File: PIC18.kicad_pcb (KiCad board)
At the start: 4 copper layers, 76.6 x 75.6 mm, 75 parts, among them J1 Conn_02x20_Odd_Even, J10 Port B, J11 Port C, J12 Port D, J13 Conn_01x03, J14 Conn_01x03, J15 Conn_01x03, J16 Conn_01x03, J2 Conn_01x06, J3 USB_A, J4 Conn_01x03, J5 Conn_01x02, J6 Conn_01x02, J7 USB_OTG, J8 Port A, J9 Port E, U1 PIC18F4620, U2 LM4040DBZ-4.1, U3 FT230XS, Y1 8 MHz

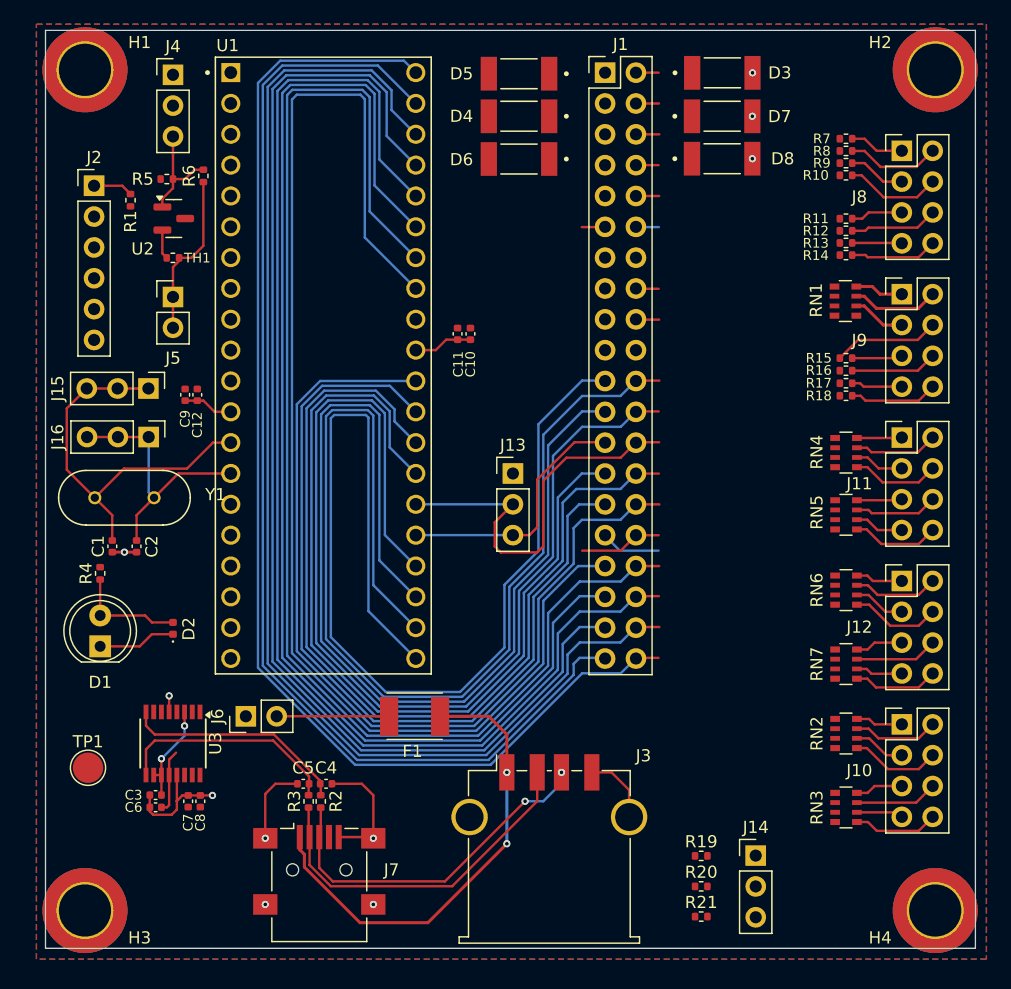
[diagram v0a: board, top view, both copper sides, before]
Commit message: Header Wiring
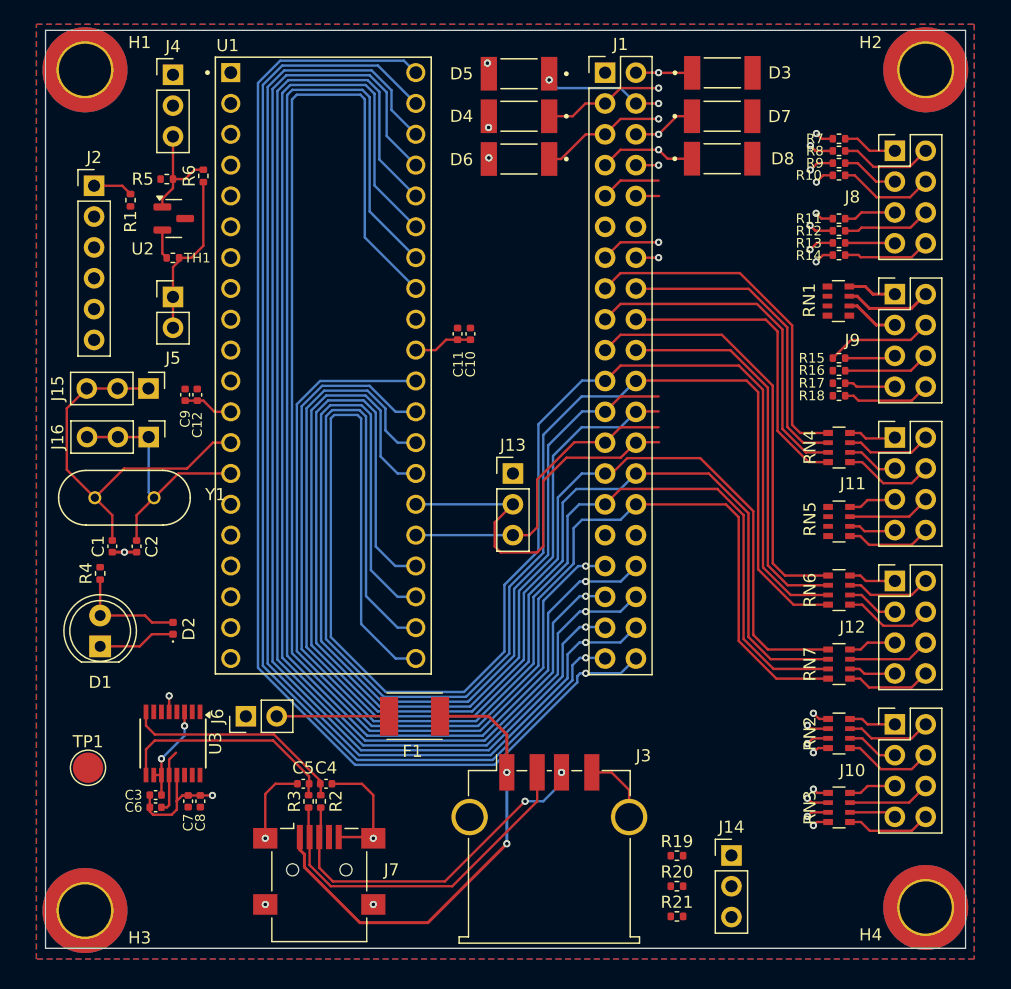
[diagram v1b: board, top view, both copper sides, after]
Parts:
- moved J14 2.00 mm to (156.0, 133.5)
- moved R19 2.00 mm to (151.5, 133.5)
- moved R20 2.00 mm to (151.5, 136.0)
- moved R21 2.00 mm to (151.5, 138.5)
- moved H4 0.82 mm to (172.0, 137.8)
- moved RN5 0.80 mm to (164.9, 106.0)
- moved H2 0.78 mm to (172.0, 68.8)
- moved RN4 0.71 mm to (164.9, 99.9)
- moved J10 0.57 mm to (169.5, 122.7)
- moved J11 0.57 mm to (169.5, 99.0)
- moved J12 0.57 mm to (169.5, 110.9)
- moved J8 0.57 mm to (169.5, 75.4)
- moved J9 0.57 mm to (169.5, 87.2)
- moved R10 0.57 mm to (164.9, 77.4)
- moved R11 0.57 mm to (164.9, 81.0)
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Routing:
- net /RB1/INT1/AN10: track 109.9 -> 149.0 mm, vias 0 -> 2
- net /RB0/INT0/FLT0/AN12: track 111.3 -> 149.9 mm, vias 0 -> 2
- net /RB3/AN9/CCP2(1): track 107.0 -> 140.8 mm, vias 0 -> 2
- net /RB2/INT2/AN8: track 108.5 -> 141.6 mm, vias 0 -> 2
- net /RD1/PSP1: track 56.3 -> 88.1 mm
- net /RD0/PSP0: track 55.6 -> 86.9 mm
- net /RD2/PSP2: track 91.9 -> 123.1 mm
- net /RD3/PSP3: track 90.5 -> 121.3 mm
- net /RB5/KBI1/PGM: track 104.1 -> 131.4 mm, vias 0 -> 2
- net /RD4/PSP4: track 78.3 -> 105.5 mm
- net /RC0/T1OSO/T13CKI: track 48.2 -> 75.3 mm
- net /RD5/PSP5/P1B: track 77.1 -> 104.0 mm
- net /RB4/KBI0/AN11: track 105.5 -> 132.0 mm, vias 0 -> 2
- net /RD6/PSP6/P1C: track 76.1 -> 102.3 mm
- net /RD7/PSP7/P1D: track 75.7 -> 101.7 mm
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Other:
- board size 76.6 x 75.6 mm -> 75.8 x 75.6 mm

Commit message: All main wiring done
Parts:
- moved R21 1.23 mm to (152.7, 138.5)
- moved R19 1.23 mm to (152.7, 133.5)
- moved R20 1.23 mm to (152.7, 136.0)
- moved J13 0.34 mm to (137.7, 102.0)
- moved J4 0.10 mm to (110.0, 69.3)
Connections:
- J13 pad 1: GND -> unconnected-(J13-Pin_1-Pad1)
- J13 pad 2: /RC7/RX/DT -> /ICTX
- J4 pad 2: /VREF+ -> /RA3/AN3/VREF+
- J4 pad 3: Net-(J4-Pin_3) -> /VREF+
- R5 pad 2: Net-(J4-Pin_3) -> /VREF+
- R6 pad 2: Net-(J4-Pin_3) -> /VREF+
- U2 pad 1: Net-(J4-Pin_3) -> /VREF+
- U3 pad 1: /RC7/RX/DT -> /ICTX
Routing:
- net /RC6/TX/CK: track 26.0 -> 155.3 mm, vias 0 -> 2
- net /VREF+: track 8.78 -> 106.8 mm, vias 0 -> 4
- net /RC7/RX/DT: track 32.7 -> 114.1 mm, vias 0 -> 2
- net /RC4/SDI/SDA: track 89.6 -> 149.7 mm, vias 0 -> 2
- net /RC5/SDO: track 88.2 -> 143.9 mm, vias 0 -> 2
- net /RC3/SCK/SCL: track 78.0 -> 130.1 mm
- net /ICTX: track 0.00 -> 39.8 mm, vias 0 -> 1
- net /RB6/KBI2/PGC: track 124.4 -> 158.1 mm, vias 2 -> 3
- net /RB7/KBI3/PGD: track 124.8 -> 158.4 mm, vias 2 -> 3
- net GND: track 53.8 -> 76.9 mm, vias 10 -> 11
- net /RE0/RD*/AN5: track 39.4 -> 57.5 mm, vias 1 -> 2
- net /RE1/WR*/AN6: track 40.0 -> 57.7 mm, vias 0 -> 2
- net /RE2/CS*/AN7: track 40.5 -> 58.1 mm, vias 0 -> 2
- net /*MCLR/VPP/RE3: track 35.2 -> 52.5 mm
- net Net-(J4-Pin_3): track 8.99 -> 0.00 mm
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
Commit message: Edited PCB
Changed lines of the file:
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@@
 	)
 	(segment
+		(start 137.65625 107.08)
+		(end 130 107.08)
+		(width 0.2)
+		(layer "In2.Cu")
+		(net 24)
+	)
+	(segment
 		(start 138.025 111.47482)
 		(end 140.825 108.67482)
@@
 	)
 	(segment
-		(start 137.65625 107.08)
-		(end 130 107.08)
-		(width 0.2)
-		(layer "B.Cu")
-		(net 24)
-	)
-	(segment
 		(start 122.968628 96.4)
 		(end 121.45 97.918628)
@@
 	)
 	(zone
-		(net 24)
-		(net_name "/RC6{slash}TX{slash}CK")
-		(layer "F.Cu")
-		(name "$teardrop_padvia$")
-		(hatch full 0.1)
-		(priority 30104)
-		(attr
-			(teardrop
-				(type padvia)
-			)
-		)
-		(connect_pads yes
-			(clearance 0)
-		)
-		(min_thickness 0.0254)
-		(filled_areas_thickness no)
-		(fill yes
-			(thermal_gap 0.5)
-			(thermal_bridge_width 0.5)
-			(island_removal_mode 1)
-			(island_area_min 10)
-		)
-		(polygon
-			(pts
-				(xy 128.815596 108.122982) (xy 128.957018 108.264404) (xy 130.301363 107.807555) (xy 130.000707 107.079293)
-				(xy 129.272445 106.778637)
-			)
-		)
-	)
-	(zone
 		(net 1)
 		(net_name "GND")
@@
 	)
 	(zone
+		(net 24)
+		(net_name "/RC6{slash}TX{slash}CK")
+		(layer "F.Cu")
+		(name "$teardrop_padvia$")
+		(hatch full 0.1)
+		(priority 30000)
+		(attr
+			(teardrop
+				(type padvia)
+			)
+		)
+		(connect_pads yes
+			(clearance 0)
+		)
+		(min_thickness 0.0254)
+		(filled_areas_thickness no)
+		(fill yes
+			(thermal_gap 0.5)
+			(thermal_bridge_width 0.5)
+			(island_removal_mode 1)
+			(island_area_min 10)
+		)
+		(polygon
+			(pts
+				(xy 128.815596 108.122982) (xy 128.957018 108.264404) (xy 130.301363 107.807555) (xy 130.000707 107.079293)
+				(xy 129.272445 106.778637)
+			)
+		)
+	)
+	(zone
 		(net 17)
 		(net_name "/RB7{slash}KBI3{slash}PGD")
@@
 	)
 	(zone
+		(net 24)
+		(net_name "/RC6{slash}TX{slash}CK")
+		(layer "In2.Cu")
+		(name "$teardrop_padvia$")
+		(hatch full 0.1)
+		(priority 30001)
+		(attr
+			(teardrop
+				(type padvia)
+			)
+		)
+		(connect_pads yes
+			(clearance 0)
+		)
+		(min_thickness 0.0254)
+		(filled_areas_thickness no)
+		(fill yes
+			(thermal_gap 0.5)
+			(thermal_bridge_width 0.5)
+			(island_removal_mode 1)
+			(island_area_min 10)
+		)
+		(polygon
+			(pts
+				(xy 131.575 107.18) (xy 131.575 106.98) (xy 130.301363 106.352445) (xy 129.999 107.08) (xy 130.301363 107.807555)
+			)
+		)
+	)
+	(zone
 		(net 38)
 		(net_name "/RA0{slash}AN0")
@@
 	)
 	(zone
+		(net 24)
+		(net_name "/RC6{slash}TX{slash}CK")
+		(layer "In2.Cu")
+		(name "$teardrop_padvia$")
+		(hatch full 0.1)
+		(priority 30000)
+		(attr
+			(teardrop
+				(type padvia)
+			)
+		)
+		(connect_pads yes
+			(clearance 0)
+		)
+		(min_thickness 0.0254)
+		(filled_areas_thickness no)
+		(fill yes
+			(thermal_gap 0.5)
+			(thermal_bridge_width 0.5)
+			(island_removal_mode 1)
+			(island_area_min 10)
+		)
+		(polygon
+			(pts
+				(xy 135.95625 106.98) (xy 135.95625 107.18) (xy 137.330969 107.865298) (xy 137.65725 107.08) (xy 137.330969 106.294702)
+			)
+		)
+	)
+	(zone
 		(net 20)
 		(net_name "/RA2{slash}AN2{slash}VREF-{slash}CVREF")
@@
 	)
 	(zone
-		(net 31)
-		(net_name "/RD6{slash}PSP6{slash}P1C")
+		(net 24)
+		(net_name "/RC6{slash}TX{slash}CK")
 		(layer "B.Cu")
 		(name "$teardrop_padvia$")
 		(hatch full 0.1)
-		(priority 30011)
+		(priority 30000)
 		(attr
 			(teardrop
@@
 		(polygon
 			(pts
-				(xy 143.892997 104.4475) (xy 143.892997 104.6475) (xy 145.267219 105.330298) (xy 145.5935 104.545)
-				(xy 145.267219 103.759702)
+				(xy 128.957018 105.895596) (xy 128.815596 106.037018) (xy 129.272445 107.381363) (xy 130.000707 107.080707)
+				(xy 130.301363 106.352445)
 			)
 		)
 	)
 	(zone
-		(net 17)
-		(net_name "/RB7{slash}KBI3{slash}PGD")
+		(net 31)
+		(net_name "/RD6{slash}PSP6{slash}P1C")
 		(layer "B.Cu")
 		(name "$teardrop_padvia$")
 		(hatch full 0.1)
-		(priority 30037)
+		(priority 30011)
 		(attr
 			(teardrop
@@
 		(polygon
 			(pts
-				(xy 128.830928 67.9) (xy 128.830928 68.1) (xy 129.272445 69.281363) (xy 130.001 68.98) (xy 130.301363 68.252445)
+				(xy 143.892997 104.4475) (xy 143.892997 104.6475) (xy 145.267219 105.330298) (xy 145.5935 104.545)
+				(xy 145.267219 103.759702)
 			)
 		)
 	)
 	(zone
-		(net 24)
-		(net_name "/RC6{slash}TX{slash}CK")
+		(net 17)
+		(net_name "/RB7{slash}KBI3{slash}PGD")
 		(layer "B.Cu")
 		(name "$teardrop_padvia$")
 		(hatch full 0.1)
-		(priority 30001)
+		(priority 30037)
 		(attr
 			(teardrop
@@
 		(polygon
 			(pts
-				(xy 143.8925 99.365) (xy 143.8925 99.565) (xy 145.267219 100.250298) (xy 145.5935 99.465) (xy 145.267219 98.679702)
+				(xy 128.830928 67.9) (xy 128.830928 68.1) (xy 129.272445 69.281363) (xy 130.001 68.98) (xy 130.301363 68.252445)
 			)
 		)
 	)
 	(zone
-		(net 9)
-		(net_name "/RD7{slash}PSP7{slash}P1D")
+		(net 24)
+		(net_name "/RC6{slash}TX{slash}CK")
 		(layer "B.Cu")
 		(name "$teardrop_padvia$")
 		(hatch full 0.1)
-		(priority 30008)
+		(priority 30001)
 		(attr
 			(teardrop
@@
 		(polygon
 			(pts
-				(xy 146.861207 105.677372) (xy 147.002628 105.818793) (xy 148.457781 105.330298) (xy 148.133207 104.544293)
-				(xy 147.347202 104.219719)
+				(xy 143.8925 99.365) (xy 143.8925 99.565) (xy 145.267219 100.250298) (xy 145.5935 99.465) (xy 145.267219 98.679702)
 			)
 		)
 	)
 	(zone
-		(net 23)
-		(net_name "/RD5{slash}PSP5{slash}P1B")
+		(net 9)
+		(net_name "/RD7{slash}PSP7{slash}P1D")
 		(layer "B.Cu")
 		(name "$teardrop_padvia$")
 		(hatch full 0.1)
-		(priority 30035)
+		(priority 30008)
 		(attr
 			(teardrop
@@
 		(polygon
 			(pts
-				(xy 128.517677 99.336257) (xy 128.376257 99.477677) (xy 129.698637 100.187555) (xy 130.000707 99.460707)
-				(xy 129.698637 98.732445)
+				(xy 146.861207 105.677372) (xy 147.002628 105.818793) (xy 148.457781 105.330298) (xy 148.133207 104.544293)
+				(xy 147.347202 104.219719)
 			)
 		)
 	)
 	(zone
-		(net 24)
-		(net_name "/RC6{slash}TX{slash}CK")
+		(net 23)
+		(net_name "/RD5{slash}PSP5{slash}P1B")
 		(layer "B.Cu")
 		(name "$teardrop_padvia$")
 		(hatch full 0.1)
-		(priority 30003)
+		(priority 30035)
 		(attr
 			(teardrop
@@
 		(polygon
 			(pts
-				(xy 135.95625 106.98) (xy 135.95625 107.18) (xy 137.330969 107.865298) (xy 137.65725 107.08) (xy 137.330969 106.294702)
+				(xy 128.517677 99.336257) (xy 128.376257 99.477677) (xy 129.698637 100.187555) (xy 130.000707 99.460707)
+				(xy 129.698637 98.732445)
 			)
 		)
@@
 	)
 	(zone
-		(net 24)
-		(net_name "/RC6{slash}TX{slash}CK")
-		(layer "B.Cu")
-		(name "$teardrop_padvia$")
-		(hatch full 0.1)
-		(priority 30032)
-		(attr
-			(teardrop
-				(type padvia)
-			)
-		)
-		(connect_pads yes
-			(clearance 0)
-		)
-		(min_thickness 0.0254)
-		(filled_areas_thickness no)
-		(fill yes
-			(thermal_gap 0.5)
-			(thermal_bridge_width 0.5)
-			(island_removal_mode 1)
-			(island_area_min 10)
-		)
-		(polygon
-			(pts
-				(xy 131.575 107.18) (xy 131.575 106.98) (xy 130.301363 106.352445) (xy 129.999 107.08) (xy 130.301363 107.807555)
-			)
-		)
-	)
-	(zone
 		(net 6)
 		(net_name "/RB5{slash}KBI1{slash}PGM")
@@
 			)
 		)
-	)
-	(zone
-		(net 24)
-		(net_name "/RC6{slash}TX{slash}CK")
-		(layer "B.Cu")
-		(name "$teardrop_padvia$")
-		(hatch full 0.1)
-		(priority 30025)
-		(attr
-			(teardrop
-				(type padvia)
-			)
-		)
-		(connect_pads yes
-			(clearance 0)
-		)
-		(min_thickness 0.0254)
-		(filled_areas_thickness no)
-		(fill yes
-			(thermal_gap 0.5)
-			(thermal_bridge_width 0.5)
-			(island_removal_mode 1)
-			(island_area_min 10)
-		)
-		(polygon
-			(pts
-				(xy 128.957018 105.895596) (xy 128.815596 106.037018) (xy 129.272445 107.381363) (xy 130.000707 107.080707)
-				(xy 130.301363 106.352445)
-			)
-		)

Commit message: Silkscreen edits
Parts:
- moved J6 1.77 mm to (117.5, 123.0)
- moved F1 1.00 mm to (129.9, 123.0)
- moved J2 0.98 mm to (103.0, 77.5)
- moved H3 0.90 mm to (102.0, 138.5)
- moved H4 0.90 mm to (172.5, 138.5)
- moved H1 0.79 mm to (102.0, 69.0)
- moved H2 0.56 mm to (172.5, 69.0)
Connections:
- net /ICTX renamed /TXD
- J13 pad 3: /RC6/TX/CK -> /RC7/RX/DT
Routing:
- net /RC7/RX/DT: track 114.1 -> 124.0 mm
- net /RC6/TX/CK: track 155.3 -> 148.7 mm
- net /RB3/AN9/CCP2(1): track 140.7 -> 146.2 mm, vias 2 -> 0
- net /RB1/INT1/AN10: track 148.0 -> 153.5 mm, vias 2 -> 0
- net /RB7/KBI3/PGD: track 158.4 -> 163.2 mm, vias 3 -> 1
- net /RB5/KBI1/PGM: track 130.5 -> 135.1 mm, vias 2 -> 0
- net /RB0/INT0/FLT0/AN12: track 148.9 -> 151.2 mm, vias 2 -> 0
- net /RB2/INT2/AN8: track 141.4 -> 143.7 mm, vias 2 -> 0
- net /RB6/KBI2/PGC: track 158.1 -> 159.8 mm, vias 3 -> 1
- net /RB4/KBI0/AN11: track 131.2 -> 132.7 mm, vias 2 -> 0
- net VCC: track 18.6 -> 17.1 mm
- net GND: track 76.9 -> 75.5 mm, vias 11 -> 13
- net Net-(J3-VBUS): track 32.7 -> 31.7 mm
- net /RD2/PSP2: track 117.2 -> 118.0 mm
- net /RD3/PSP3: track 115.4 -> 116.2 mm
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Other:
- board size 75.8 x 75.6 mm -> 76.5 x 75.5 mm
- board text added: "+5V"
- board text added: "Designed by pixelated_knight"
- board text added: "ICTX"
- board text added: "MC VREF+"
- board text added: "MCRX"
- board text added: "PICKIT4"
- board text added: "PORT A"
- board text added: "PORT B"
- board text added: "PORT C"
- board text added: "PORT D"
- board text added: "PORT E"
- board text added: "SCL"
- board text added: "SDI"
- board text added: "SDO"
- board text added: "VREF+"
- board text added: "VTH"

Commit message: JLCPCB parody edits
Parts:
- C10, C12: value .1uf -> 100nf

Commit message: more jlcpcb parody
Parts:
- D2: footprint LED_SMD:LED_0402_1005Metric -> LED_SMD:LED_0805_2012Metric
- R2, R3: value 27 -> 33
- moved D2 0.19 mm to (110.0, 114.9)

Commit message: prod
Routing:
- net /RD7/PSP7/P1D: track 102.2 -> 101.6 mm

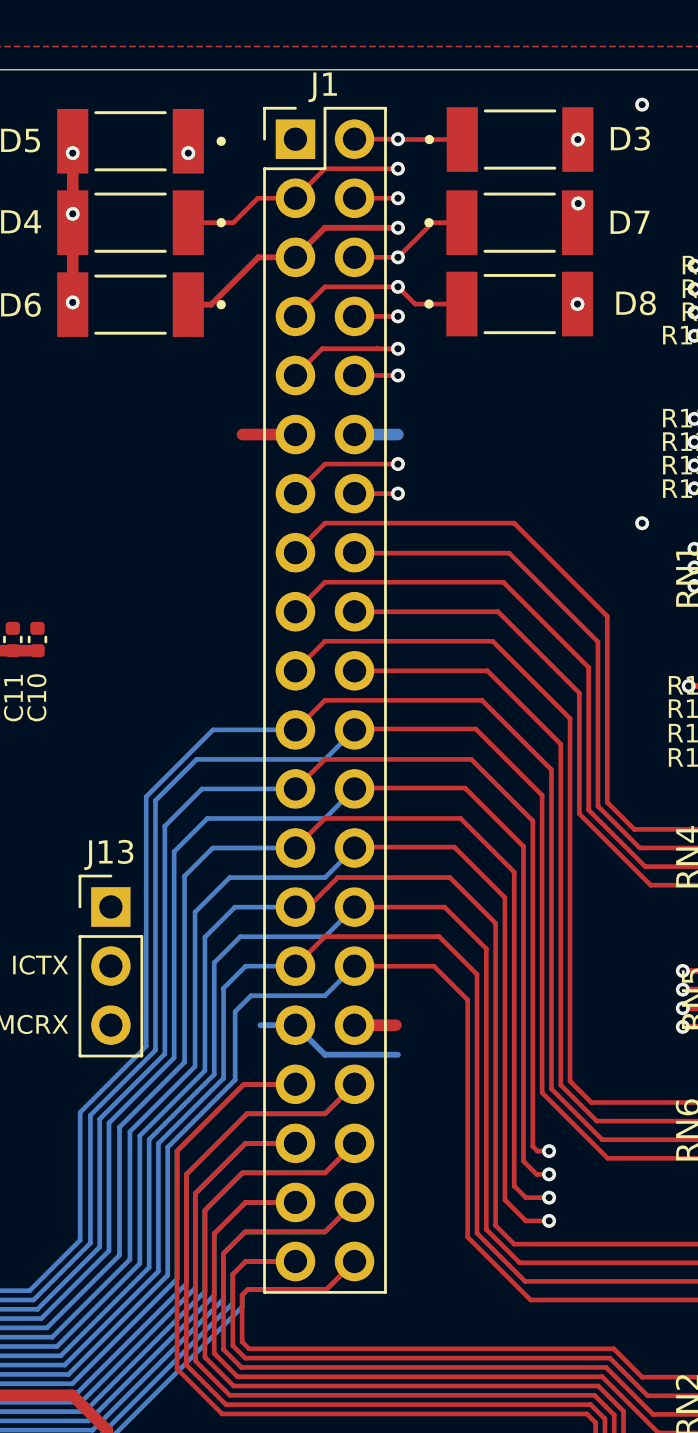
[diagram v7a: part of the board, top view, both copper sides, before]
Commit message: Changed main pin header to pin socket
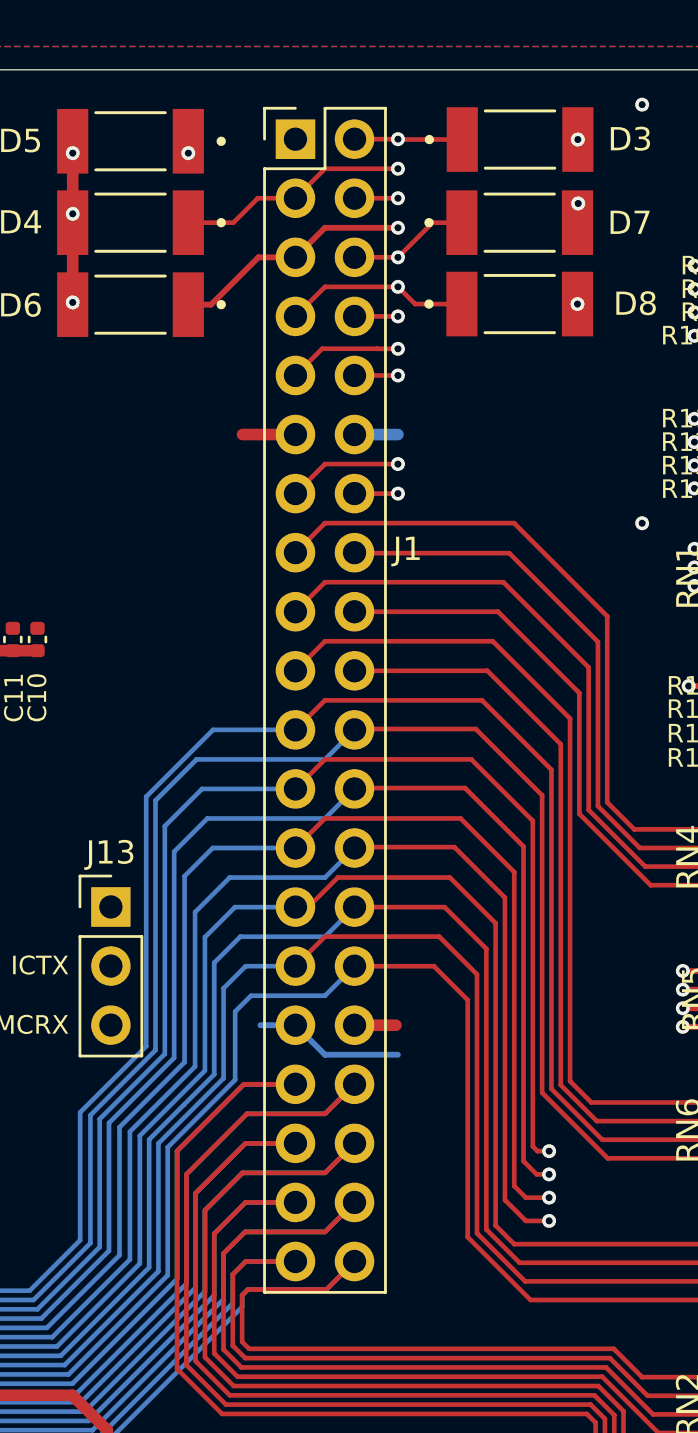
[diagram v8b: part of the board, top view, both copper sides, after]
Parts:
- J1: footprint Connector_PinHeader_2.54mm:PinHeader_2x20_P2.54mm_Vertical -> PinSockets:PinSocket_2x20_Counter_Clockwise_P2.54mm_Vertical
- moved J1 2.54 mm to (148.1, 69.0)
